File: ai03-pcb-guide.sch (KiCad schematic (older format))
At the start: 1 part

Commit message: First components
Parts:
- added R?: 10k, symbol Device:R_Small
- added R? (x2): 22, symbol Device:R_Small
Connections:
- wire segments 5 -> 11
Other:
- moved on the sheet: U?
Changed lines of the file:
@@
 L power:+5V #PWR?
 U 1 1 6034AA97
-P 1250 600
-F 0 "#PWR?" H 1250 450 50  0001 C CNN
-F 1 "+5V" H 1265 773 50  0000 C CNN
-F 2 "" H 1250 600 50  0001 C CNN
-F 3 "" H 1250 600 50  0001 C CNN
-	1    1250 600
+P 3400 1850
+F 0 "#PWR?" H 3400 1700 50  0001 C CNN
+F 1 "+5V" H 3415 2023 50  0000 C CNN
+F 2 "" H 3400 1850 50  0001 C CNN
+F 3 "" H 3400 1850 50  0001 C CNN
+	1    3400 1850
 	1    0    0    -1
 $EndComp
@@
 L MCU_Microchip_ATmega:ATmega32U4-AU U?
 U 1 1 603422EB
-P 1350 2550
-F 0 "U?" H 1350 661 50  0000 C CNN
-F 1 "ATmega32U4-AU" H 1350 570 50  0000 C CNN
-F 2 "Package_QFP:TQFP-44_10x10mm_P0.8mm" H 1350 2550 50  0001 C CIN
-F 3 "http://ww1.microchip.com/downloads/en/DeviceDoc/Atmel-7766-8-bit-AVR-ATmega16U4-32U4_Datasheet.pdf" H 1350 2550 50  0001 C CNN
-	1    1350 2550
+P 3500 3800
+F 0 "U?" H 3500 1911 50  0000 C CNN
+F 1 "ATmega32U4-AU" H 3500 1820 50  0000 C CNN
+F 2 "Package_QFP:TQFP-44_10x10mm_P0.8mm" H 3500 3800 50  0001 C CIN
+F 3 "http://ww1.microchip.com/downloads/en/DeviceDoc/Atmel-7766-8-bit-AVR-ATmega16U4-32U4_Datasheet.pdf" H 3500 3800 50  0001 C CNN
+	1    3500 3800
 	1    0    0    -1
 $EndComp
 Wire Wire Line
-	1250 600  1250 750
+	3400 1850 3400 2000
 Wire Wire Line
-	1250 750  1350 750
-Connection ~ 1250 750
-Connection ~ 1350 750
+	3400 2000 3500 2000
+Connection ~ 3400 2000
+Connection ~ 3500 2000
 Wire Wire Line
-	1350 750  1450 750
+	3500 2000 3600 2000
 $Comp
 L power:GND #PWR?
 U 1 1 60353577
-P 900 4350
-F 0 "#PWR?" H 900 4100 50  0001 C CNN
-F 1 "GND" H 905 4177 50  0000 C CNN
-F 2 "" H 900 4350 50  0001 C CNN
-F 3 "" H 900 4350 50  0001 C CNN
-	1    900  4350
+P 3050 5600
+F 0 "#PWR?" H 3050 5350 50  0001 C CNN
+F 1 "GND" H 3055 5427 50  0000 C CNN
+F 2 "" H 3050 5600 50  0001 C CNN
+F 3 "" H 3050 5600 50  0001 C CNN
+	1    3050 5600
 	1    0    0    -1
 $EndComp
 Wire Wire Line
-	900  4350 1250 4350
-Connection ~ 1250 4350
+	3050 5600 3400 5600
+Connection ~ 3400 5600
 Wire Wire Line
-	1250 4350 1350 4350
+	3400 5600 3500 5600
+$Comp
+L Device:R_Small R?
+U 1 1 60354F38
+P 4500 4400
+F 0 "R?" V 4304 4400 50  0000 C CNN
+F 1 "10k" V 4395 4400 50  0000 C CNN
+F 2 "" H 4500 4400 50  0001 C CNN
+F 3 "~" H 4500 4400 50  0001 C CNN
+	1    4500 4400
+	0    1    1    0
+$EndComp
+$Comp
+L power:GND #PWR?
+U 1 1 60356495
+P 4950 4400
+F 0 "#PWR?" H 4950 4150 50  0001 C CNN
+F 1 "GND" H 4955 4227 50  0000 C CNN
+F 2 "" H 4950 4400 50  0001 C CNN
+F 3 "" H 4950 4400 50  0001 C CNN
+	1    4950 4400
+	1    0    0    -1
+$EndComp
+Wire Wire Line
+	4100 4400 4400 4400
+Wire Wire Line
+	4600 4400 4950 4400
+$Comp
+L Device:R_Small R?
+U 1 1 60365BE5
+P 2200 3400
+F 0 "R?" V 2004 3400 50  0000 C CNN
+F 1 "22" V 2095 3400 50  0000 C CNN
+F 2 "" H 2200 3400 50  0001 C CNN
+F 3 "~" H 2200 3400 50  0001 C CNN
+	1    2200 3400
+	0    1    1    0
+$EndComp
+Wire Wire Line
+	2900 3300 2600 3300
+Wire Wire Line
+	2400 3300 1850 3300
+Wire Wire Line
+	2100 3400 1850 3400
+Wire Wire Line
+	2900 3400 2300 3400
+$Comp
+L Device:R_Small R?
+U 1 1 6036534E
+P 2500 3300
+F 0 "R?" V 2304 3300 50  0000 C CNN
+F 1 "22" V 2395 3300 50  0000 C CNN
+F 2 "" H 2500 3300 50  0001 C CNN
+F 3 "~" H 2500 3300 50  0001 C CNN
+	1    2500 3300
+	0    1    1    0
+$EndComp
 $EndSCHEMATC

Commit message: Complete MCU
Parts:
- added C? (x3): 0.1uF, symbol Device:C_Small
- added C?: 10uF, symbol Device:C_Small
- added C? (x2): 22pF, symbol Device:C_Small
- added C?: 1uF, symbol Device:C_Small
- added R?: 10k, symbol Device:R_Small
- added SW?: SW_Push, symbol Switch:SW_Push
- added Y?: 16MHz, symbol Device:Crystal_GND24_Small
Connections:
- net labels added: D+, D-
- wire segments 11 -> 41

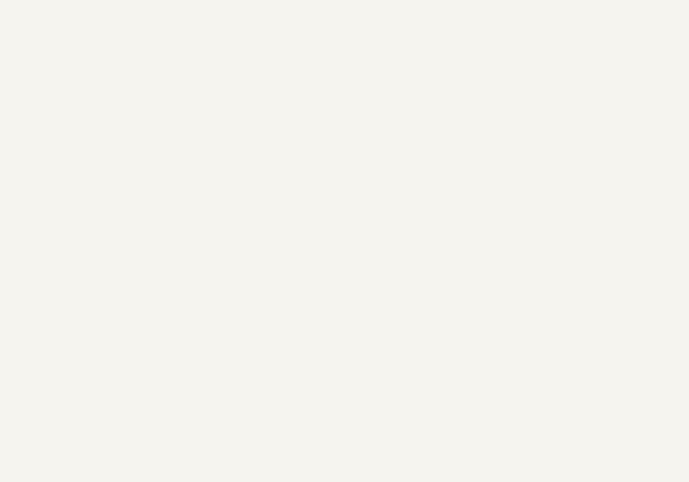
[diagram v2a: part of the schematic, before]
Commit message: USB Mini-B connector
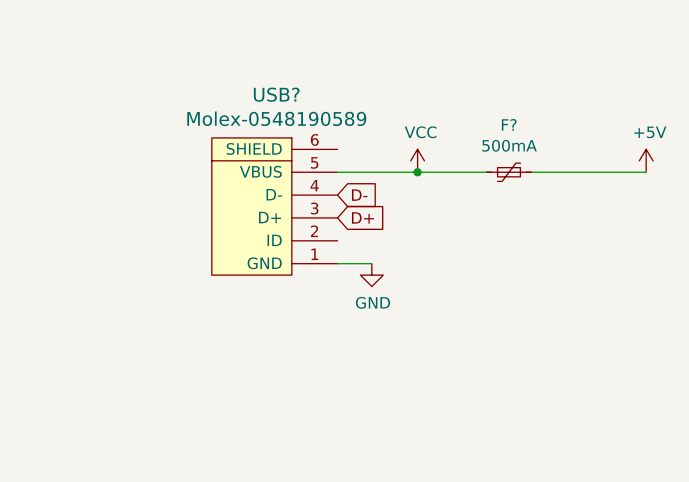
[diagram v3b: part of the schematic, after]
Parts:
- added F?: 500mA, symbol Device:Polyfuse_Small
- added USB?: Molex-0548190589, symbol random-keyboard-parts:Molex-0548190589
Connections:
- net labels added: VCC
- wire segments 41 -> 45
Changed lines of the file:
@@
 Wire Wire Line
 	2550 3800 2550 3900
+$Comp
+L random-keyboard-parts:Molex-0548190589 USB?
+U 1 1 6038615F
+P 6300 2400
+F 0 "USB?" V 6837 2367 60  0000 C CNN
+F 1 "Molex-0548190589" V 6731 2367 60  0000 C CNN
+F 2 "" H 6300 2400 60  0001 C CNN
+F 3 "" H 6300 2400 60  0001 C CNN
+	1    6300 2400
+	0    -1   -1   0
+$EndComp
+$Comp
+L Device:Polyfuse_Small F?
+U 1 1 60388AFC
+P 7350 2200
+F 0 "F?" V 7145 2200 50  0000 C CNN
+F 1 "500mA" V 7236 2200 50  0000 C CNN
+F 2 "" H 7400 2000 50  0001 L CNN
+F 3 "~" H 7350 2200 50  0001 C CNN
+	1    7350 2200
+	0    1    1    0
+$EndComp
+Wire Wire Line
+	6600 2200 6950 2200
+$Comp
+L power:VCC #PWR?
+U 1 1 6038C6B9
+P 6950 2200
+F 0 "#PWR?" H 6950 2050 50  0001 C CNN
+F 1 "VCC" H 6965 2373 50  0000 C CNN
+F 2 "" H 6950 2200 50  0001 C CNN
+F 3 "" H 6950 2200 50  0001 C CNN
+	1    6950 2200
+	1    0    0    -1
+$EndComp
+Connection ~ 6950 2200
+Wire Wire Line
+	6950 2200 7250 2200
+Wire Wire Line
+	7450 2200 7950 2200
+$Comp
+L power:+5V #PWR?
+U 1 1 6038A873
+P 7950 2200
+F 0 "#PWR?" H 7950 2050 50  0001 C CNN
+F 1 "+5V" H 7965 2373 50  0000 C CNN
+F 2 "" H 7950 2200 50  0001 C CNN
+F 3 "" H 7950 2200 50  0001 C CNN
+	1    7950 2200
+	1    0    0    -1
+$EndComp
+Text GLabel 6600 2400 2    50   Input ~ 0
+D+
+Text GLabel 6600 2300 2    50   Input ~ 0
+D-
+$Comp
+L power:GND #PWR?
+U 1 1 60394008
+P 6750 2600
+F 0 "#PWR?" H 6750 2350 50  0001 C CNN
+F 1 "GND" H 6755 2427 50  0000 C CNN
+F 2 "" H 6750 2600 50  0001 C CNN
+F 3 "" H 6750 2600 50  0001 C CNN
+	1    6750 2600
+	1    0    0    -1
+$EndComp
+Wire Wire Line
+	6600 2600 6750 2600
 $EndSCHEMATC

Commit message: Switch schematic
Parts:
- added D? (x4): SOD-123, symbol Device:D_Small
- added MX? (x4): MX-NoLED, symbol MX_Alps_Hybrid:MX-NoLED
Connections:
- net labels added: COL0, COL1, ROW0, ROW1
- wire segments 45 -> 57
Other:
- moved on the sheet: F?, USB?
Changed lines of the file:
@@
 L random-keyboard-parts:Molex-0548190589 USB?
 U 1 1 6038615F
-P 6300 2400
-F 0 "USB?" V 6837 2367 60  0000 C CNN
-F 1 "Molex-0548190589" V 6731 2367 60  0000 C CNN
-F 2 "" H 6300 2400 60  0001 C CNN
-F 3 "" H 6300 2400 60  0001 C CNN
-	1    6300 2400
+P 5450 2450
+F 0 "USB?" V 5987 2417 60  0000 C CNN
+F 1 "Molex-0548190589" V 5881 2417 60  0000 C CNN
+F 2 "" H 5450 2450 60  0001 C CNN
+F 3 "" H 5450 2450 60  0001 C CNN
+	1    5450 2450
 	0    -1   -1   0
 $EndComp
@@
 L Device:Polyfuse_Small F?
 U 1 1 60388AFC
-P 7350 2200
-F 0 "F?" V 7145 2200 50  0000 C CNN
-F 1 "500mA" V 7236 2200 50  0000 C CNN
-F 2 "" H 7400 2000 50  0001 L CNN
-F 3 "~" H 7350 2200 50  0001 C CNN
-	1    7350 2200
+P 6500 2250
+F 0 "F?" V 6295 2250 50  0000 C CNN
+F 1 "500mA" V 6386 2250 50  0000 C CNN
+F 2 "" H 6550 2050 50  0001 L CNN
+F 3 "~" H 6500 2250 50  0001 C CNN
+	1    6500 2250
 	0    1    1    0
 $EndComp
 Wire Wire Line
-	6600 2200 6950 2200
+	5750 2250 6100 2250
 $Comp
 L power:VCC #PWR?
 U 1 1 6038C6B9
-P 6950 2200
-F 0 "#PWR?" H 6950 2050 50  0001 C CNN
-F 1 "VCC" H 6965 2373 50  0000 C CNN
-F 2 "" H 6950 2200 50  0001 C CNN
-F 3 "" H 6950 2200 50  0001 C CNN
-	1    6950 2200
+P 6100 2250
+F 0 "#PWR?" H 6100 2100 50  0001 C CNN
+F 1 "VCC" H 6115 2423 50  0000 C CNN
+F 2 "" H 6100 2250 50  0001 C CNN
+F 3 "" H 6100 2250 50  0001 C CNN
+	1    6100 2250
 	1    0    0    -1
 $EndComp
-Connection ~ 6950 2200
+Connection ~ 6100 2250
 Wire Wire Line
-	6950 2200 7250 2200
+	6100 2250 6400 2250
 Wire Wire Line
-	7450 2200 7950 2200
+	6600 2250 7100 2250
 $Comp
 L power:+5V #PWR?
 U 1 1 6038A873
-P 7950 2200
-F 0 "#PWR?" H 7950 2050 50  0001 C CNN
-F 1 "+5V" H 7965 2373 50  0000 C CNN
-F 2 "" H 7950 2200 50  0001 C CNN
-F 3 "" H 7950 2200 50  0001 C CNN
-	1    7950 2200
+P 7100 2250
+F 0 "#PWR?" H 7100 2100 50  0001 C CNN
+F 1 "+5V" H 7115 2423 50  0000 C CNN
+F 2 "" H 7100 2250 50  0001 C CNN
+F 3 "" H 7100 2250 50  0001 C CNN
+	1    7100 2250
 	1    0    0    -1
 $EndComp
-Text GLabel 6600 2400 2    50   Input ~ 0
+Text GLabel 5750 2450 2    50   Input ~ 0
 D+
-Text GLabel 6600 2300 2    50   Input ~ 0
+Text GLabel 5750 2350 2    50   Input ~ 0
 D-
 $Comp
 L power:GND #PWR?
 U 1 1 60394008
-P 6750 2600
-F 0 "#PWR?" H 6750 2350 50  0001 C CNN
-F 1 "GND" H 6755 2427 50  0000 C CNN
-F 2 "" H 6750 2600 50  0001 C CNN
-F 3 "" H 6750 2600 50  0001 C CNN
-	1    6750 2600
+P 5900 2650
+F 0 "#PWR?" H 5900 2400 50  0001 C CNN
+F 1 "GND" H 5905 2477 50  0000 C CNN
+F 2 "" H 5900 2650 50  0001 C CNN
+F 3 "" H 5900 2650 50  0001 C CNN
+	1    5900 2650
 	1    0    0    -1
 $EndComp
 Wire Wire Line
-	6600 2600 6750 2600
+	5750 2650 5900 2650
+$Comp
+L MX_Alps_Hybrid:MX-NoLED MX?
+U 1 1 60395692
+P 6250 3900
+F 0 "MX?" H 6283 4123 60  0000 C CNN
+F 1 "MX-NoLED" H 6283 4049 20  0000 C CNN
+F 2 "" H 5625 3875 60  0001 C CNN
+F 3 "" H 5625 3875 60  0001 C CNN
+	1    6250 3900
+	1    0    0    -1
+$EndComp
+$Comp
+L Device:D_Small D?
+U 1 1 6039B382
+P 6000 4150
+F 0 "D?" V 6046 4080 50  0000 R CNN
+F 1 "SOD-123" V 5955 4080 50  0000 R CNN
+F 2 "" V 6000 4150 50  0001 C CNN
+F 3 "~" V 6000 4150 50  0001 C CNN
+	1    6000 4150
+	0    -1   -1   0
+$EndComp
+Wire Wire Line
+	6200 4050 6000 4050
+$Comp
+L MX_Alps_Hybrid:MX-NoLED MX?
+U 1 1 603A0BDE
+P 6950 3900
+F 0 "MX?" H 6983 4123 60  0000 C CNN
+F 1 "MX-NoLED" H 6983 4049 20  0000 C CNN
+F 2 "" H 6325 3875 60  0001 C CNN
+F 3 "" H 6325 3875 60  0001 C CNN
+	1    6950 3900
+	1    0    0    -1
+$EndComp
+$Comp
+L Device:D_Small D?
+U 1 1 603A17C0
+P 6700 4150
+F 0 "D?" V 6746 4080 50  0000 R CNN
+F 1 "SOD-123" V 6655 4080 50  0000 R CNN
+F 2 "" V 6700 4150 50  0001 C CNN
+F 3 "~" V 6700 4150 50  0001 C CNN
+	1    6700 4150
+	0    -1   -1   0
+$EndComp
+Wire Wire Line
+	6900 4050 6700 4050
+$Comp
+L MX_Alps_Hybrid:MX-NoLED MX?
+U 1 1 603A2C50
+P 6250 4650
+F 0 "MX?" H 6283 4873 60  0000 C CNN
+F 1 "MX-NoLED" H 6283 4799 20  0000 C CNN
+F 2 "" H 5625 4625 60  0001 C CNN
+F 3 "" H 5625 4625 60  0001 C CNN
+	1    6250 4650
+	1    0    0    -1
+$EndComp
+$Comp
+L Device:D_Small D?
+U 1 1 603A36D6
+P 6000 4900
+F 0 "D?" V 6046 4830 50  0000 R CNN
+F 1 "SOD-123" V 5955 4830 50  0000 R CNN
+F 2 "" V 6000 4900 50  0001 C CNN
+F 3 "~" V 6000 4900 50  0001 C CNN
+	1    6000 4900
+	0    -1   -1   0
+$EndComp
+Wire Wire Line
+	6200 4800 6000 4800
+$Comp
+L MX_Alps_Hybrid:MX-NoLED MX?
+U 1 1 603A4940
+P 6950 4650
+F 0 "MX?" H 6983 4873 60  0000 C CNN
+F 1 "MX-NoLED" H 6983 4799 20  0000 C CNN
+F 2 "" H 6325 4625 60  0001 C CNN
+F 3 "" H 6325 4625 60  0001 C CNN
+	1    6950 4650
+	1    0    0    -1
+$EndComp
+$Comp
+L Device:D_Small D?
+U 1 1 603A51B7
+P 6700 4900
+F 0 "D?" V 6746 4830 50  0000 R CNN
+F 1 "SOD-123" V 6655 4830 50  0000 R CNN
+F 2 "" V 6700 4900 50  0001 C CNN
+F 3 "~" V 6700 4900 50  0001 C CNN
+	1    6700 4900
+	0    -1   -1   0
+$EndComp
+Wire Wire Line
+	6900 4800 6700 4800
+Wire Wire Line
+	7100 4600 7100 3850
+Connection ~ 7100 3850
+Wire Wire Line
+	7100 3850 7100 3250
+Wire Wire Line
+	6400 4600 6400 3850
+Connection ~ 6400 3850
+Wire Wire Line
+	6400 3850 6400 3250
+Wire Wire Line
+	6700 4250 6000 4250
+Connection ~ 6000 4250
+Wire Wire Line
+	6000 4250 5650 4250
+Wire Wire Line
+	6700 5000 6000 5000
+Connection ~ 6000 5000
+Wire Wire Line
+	6000 5000 5650 5000
+Text GLabel 6400 3250 1    50   Input ~ 0
+COL0
+Text GLabel 7100 3250 1    50   Input ~ 0
+COL1
+Text GLabel 5650 4250 0    50   Input ~ 0
+ROW0
+Text GLabel 5650 5000 0    50   Input ~ 0
+ROW1
 $EndSCHEMATC

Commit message: Assigning footprints
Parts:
- C1, C2, C3, C4, C5, C6, C7: renamed from C?; footprint (none) -> Capacitor_SMD:C_0805_2012Metric
- D1, D2, D3, D4: renamed from D?; footprint (none) -> Diode_SMD:D_SOD-123
- F1: renamed from F?; footprint (none) -> Fuse:Fuse_1206_3216Metric
- MX1, MX2, MX3, MX4: renamed from MX?; footprint (none) -> MX_Alps_Hybrid:MX-1U-NoLED
- R1, R2, R3, R4: renamed from R?; footprint (none) -> Resistor_SMD:R_0805_2012Metric
- SW1: renamed from SW?; footprint (none) -> random-keyboard-parts:SKQG-1155865
- USB1: renamed from USB?; footprint (none) -> random-keyboard-parts:Molex-0548190589
- Y1: renamed from Y?; footprint (none) -> Crystal:Crystal_SMD_3225-4Pin_3.2x2.5mm
- gave numbers to parts that had none: 1

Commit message: Route to switches
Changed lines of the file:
@@
 Text GLabel 5650 5000 0    50   Input ~ 0
 ROW1
+Text GLabel 4100 2700 2    50   Input ~ 0
+COL1
+Text GLabel 4100 2800 2    50   Input ~ 0
+ROW0
+Text GLabel 4100 2900 2    50   Input ~ 0
+ROW1
+Text GLabel 4100 4200 2    50   Input ~ 0
+COL0
 $EndSCHEMATC
